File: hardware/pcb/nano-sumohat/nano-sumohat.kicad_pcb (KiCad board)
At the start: 2 copper layers, 59.7 x 30.5 mm, 14 parts, among them J1 Analog, J10 H-OUT, J2 Digital, J4 IR-B, J5 IR-F, J6 UltrSnd, J7 H, J8 IR-START, J9 BAT-IN, SW1 Power SW

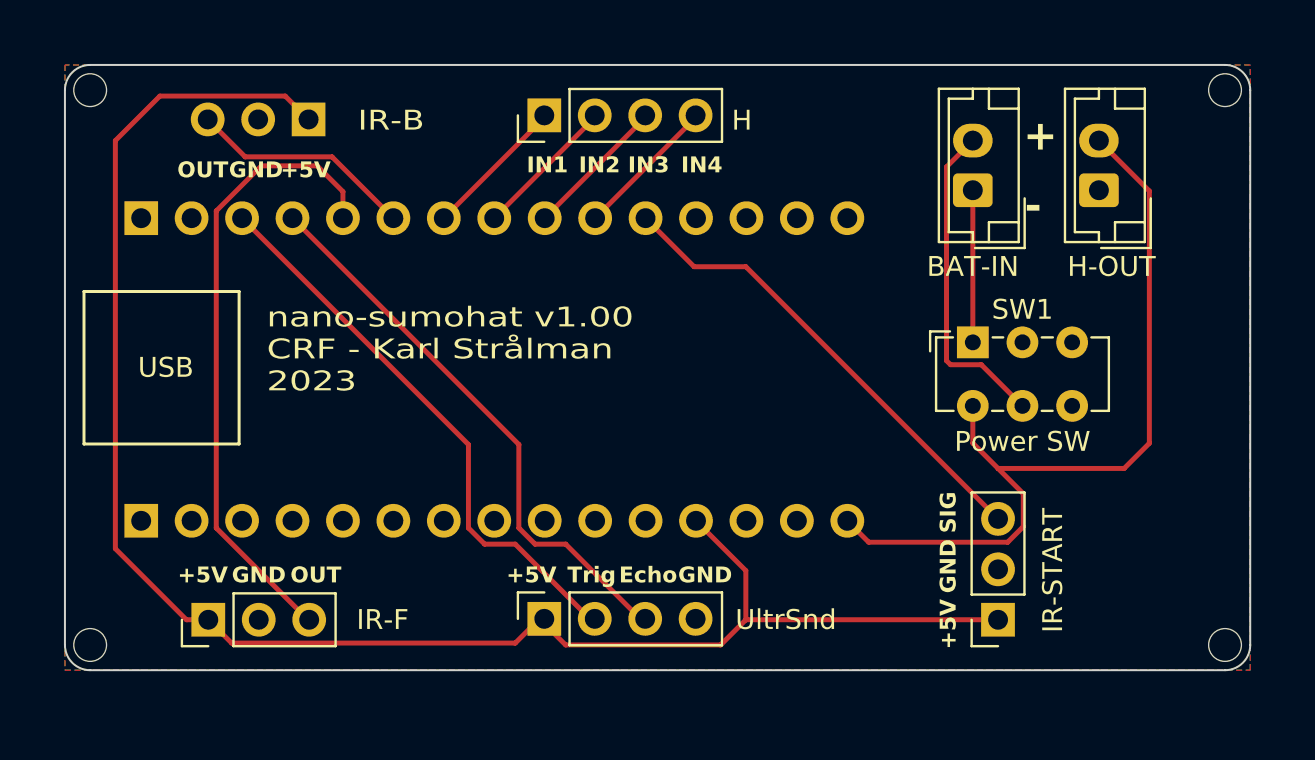
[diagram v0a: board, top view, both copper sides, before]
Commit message: Add v1.1 for nano sumohat
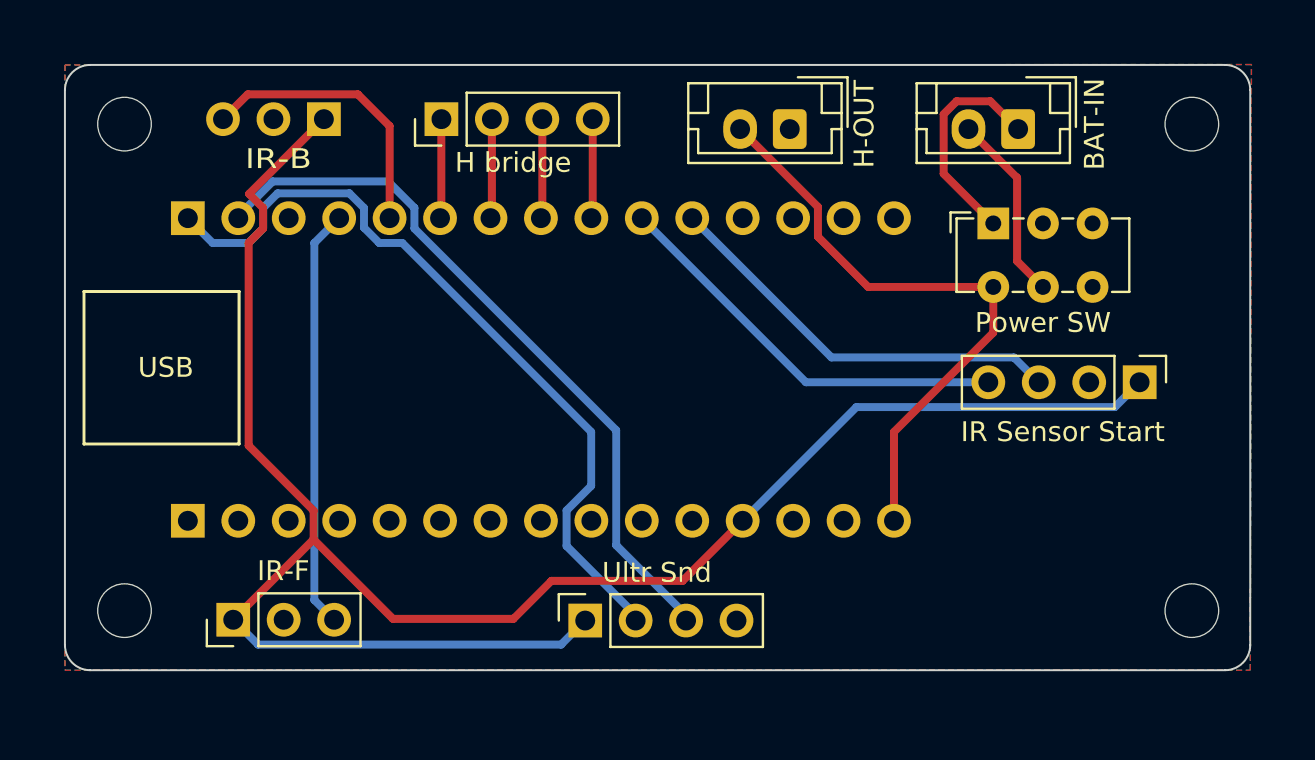
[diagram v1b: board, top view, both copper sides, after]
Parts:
- removed J8: IR-START, Connector_PinSocket_2.54mm:PinSocket_1x03_P2.54mm_Vertical
- removed MH1, MH2, MH3, MH4: MountingHole_65mil, Arduino_MountingHole:MountingHole_65mil
- added G***: LOGO, crf:crf_15x15, B.Cu at (116.8, 85.0)
- added J3: IR Sensor Start, Connector_PinHeader_2.54mm:PinHeader_1x04_P2.54mm_Vertical, F.Cu at (154.1, 85.5)
- added REF**: MountingHole_2.7mm_M2.5, MountingHole:MountingHole_2.7mm_M2.5, F.Cu at (156.8, 97.0)
- added REF**: MountingHole_2.7mm_M2.5, MountingHole:MountingHole_2.7mm_M2.5, F.Cu at (156.8, 72.5)
- added REF**: MountingHole_2.7mm_M2.5, MountingHole:MountingHole_2.7mm_M2.5, F.Cu at (103.0, 97.0)
- added REF**: MountingHole_2.7mm_M2.5, MountingHole:MountingHole_2.7mm_M2.5, F.Cu at (103.0, 72.5)
- J6: value UltrSnd -> Ultr Snd
- J7: value H -> H bridge
- moved J10 15.9 mm to (136.5, 72.8), turned to 180 degrees
- moved SW1 6.08 mm to (146.8, 77.5)
- moved J7 5.18 mm to (119.0, 72.2)
- moved J9 3.83 mm to (148.0, 72.8), turned to 180 degrees
- moved J1 2.35 mm to (106.2, 92.5)
- moved J2 2.35 mm to (106.2, 77.2)
- moved J6 2.06 mm to (126.2, 97.5)
- moved J5 1.25 mm to (108.5, 97.5)
- moved J4 0.77 mm to (113.0, 72.2)
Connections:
- J4 pad 3: /D7 -> /D8
- J5 pad 3: /D8 -> /*D9
- J6 pad 2: /*D10/SS -> /D12/MISO
- J6 pad 3: /*D9 -> /*D11/MOSI
- J7 pad 1: /*D6 -> /D7
- J7 pad 2: /*D5 -> /*D6
- J7 pad 3: /D4 -> /*D5
- J7 pad 4: /*D3 -> /D4
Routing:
- net /D12/MISO: track 0.00 -> 39.5 mm
- net /*D11/MOSI: track 0.00 -> 36.7 mm
- net /*D10/SS: track 28.3 -> 0.00 mm
- net /D8: track 31.8 -> 14.2 mm
- net /*D3: track 7.27 -> 20.9 mm
- net +5V: track 85.7 -> 97.3 mm
- net VCC: track 41.2 -> 30.8 mm
- net /*D9: track 28.3 -> 21.2 mm
- net /BAT_VCC: track 16.4 -> 9.50 mm
- net /D7: track 11.4 -> 5.02 mm
- net /BAT_GND: track 7.66 -> 11.1 mm
- net /D2: track 24.0 -> 20.9 mm
- net /*D6: track 7.27 -> 5.09 mm
- net /D4: track 7.27 -> 5.21 mm
- net /*D5: track 7.27 -> 5.28 mm
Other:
- board text added: "B_GND"
- board text added: "B_VCC"
- board text added: "Kill"
- board text added: "Start"
- board text added: "VCC"
- board text added: "nano-sumohat v1.1 Karl Strålman 2024-03"
- board text removed: "SIG"
- board text removed: "nano-sumohat v1.00 CRF - Karl Strålman 2023"

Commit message: Add v2-draft6 build guide
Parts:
- removed REF** (x4): MountingHole_2.7mm_M2.5, MountingHole:MountingHole_2.7mm_M2.5
- added G***: LOGO, crf:crf_15x15, F.Cu at (116.8, 85.0)
- added H1: MountingHole, MountingHole:MountingHole_2.7mm_M2.5_DIN965_Pad_TopBottom, F.Cu at (103.9, 87.5)
- added H2: MountingHole, MountingHole:MountingHole_2.7mm_M2.5_DIN965_Pad_TopBottom, F.Cu at (156.0, 73.1)
- added H3: MountingHole, MountingHole:MountingHole_2.7mm_M2.5_DIN965_Pad_TopBottom, F.Cu at (155.4, 87.5)
- added H4: MountingHole, MountingHole:MountingHole_2.7mm_M2.5_DIN965_Pad_TopBottom, F.Cu at (103.4, 72.9)
- added J8: Extension, Connector_PinHeader_2.54mm:PinHeader_2x05_P2.54mm_Vertical, F.Cu at (147.3, 97.5)
- added SW2: ~, Button_Switch_THT:SW_Slide-03_Wuerth-WS-SLTV_10x2.5x6.4_P2.54mm, F.Cu at (116.9, 97.5)
- J3: value IR Sensor Start -> IR_START
- J4: value IR-B -> IR_B
- J5: value IR-F -> IR_F
- J6: value Ultr Snd -> SND_Sensor
- J7: value H bridge -> Motor; footprint Connector_PinHeader_2.54mm:PinHeader_1x04_P2.54mm_Vertical -> Connector_PinHeader_2.54mm:PinHeader_1x06_P2.54mm_Vertical
- moved J4 21.1 mm to (134.1, 72.0)
- moved J7 6.26 mm to (112.7, 72.1)
- moved J5 5.50 mm to (103.0, 97.4)
- moved J10 5.36 mm to (141.8, 72.5)
- moved SW1 5.27 mm to (152.0, 77.0)
- moved J3 4.38 mm to (157.8, 83.0)
- moved J9 2.40 mm to (150.4, 72.5)
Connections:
- J3 pad 3: /D2 -> /START
- J7 pad 1: /D7 -> /A6
- J7 pad 2: /*D6 -> /D7
- J7 pad 3: /*D5 -> /*D6
- J7 pad 4: /D4 -> /*D5
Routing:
- net /D13/SCK: track 0.00 -> 67.6 mm, vias 0 -> 4
- net /*D10/SS: track 0.00 -> 66.8 mm, vias 0 -> 3
- net /START: track 0.00 -> 48.9 mm
- net /A2: track 0.00 -> 44.9 mm, vias 0 -> 2
- net /A0: track 0.00 -> 43.4 mm, vias 0 -> 2
- net /A3: track 0.00 -> 42.5 mm, vias 0 -> 3
- net /A1: track 0.00 -> 42.2 mm, vias 0 -> 5
- net /A5/SCL: track 0.00 -> 42.1 mm, vias 0 -> 5
- net /A4/SDA: track 0.00 -> 34.4 mm, vias 0 -> 1
- net /A6: track 0.00 -> 30.6 mm
- net +5V: track 97.3 -> 73.0 mm
- net /D0/RX: track 0.00 -> 24.0 mm, vias 0 -> 2
- net /A7: track 0.00 -> 23.0 mm
- net /D1/TX: track 0.00 -> 20.1 mm, vias 0 -> 2
- net /D8: track 14.2 -> 0.00 mm
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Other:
- board text added: "ENA"
- board text added: "ENB"
- board text added: "Start SEL"
- board text added: "nano-sumohat v1.2 Karl Strålman 2024-09"
- board text removed: "USB"
- board text removed: "nano-sumohat v1.1 Karl Strålman 2024-03"

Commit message: Update PCB v1.2
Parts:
- SW1: value Power SW -> ~; footprint Button_Switch_THT:SW_E-Switch_EG1271_SPDT -> Button_Switch_THT:SW_Slide-03_Wuerth-WS-SLTV_10x2.5x6.4_P2.54mm
- moved SW1 2.90 mm to (153.5, 79.5)
- moved H1 0.63 mm to (103.5, 88.0)
- moved H2 0.51 mm to (156.5, 73.0)
- moved H3 0.51 mm to (155.5, 88.0)
- moved H4 0.17 mm to (103.5, 73.0)
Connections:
- J9 pad 1: /BAT_GND -> GND
- SW1 pad 1: /BAT_GND -> /BAT_VCC
- SW1 pad 2: GND -> unconnected-(SW1-C-Pad2)
- SW1 pad 3: unconnected-(SW1-Pad3) -> VCC
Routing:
- net /D8: track 0.00 -> 17.2 mm, vias 0 -> 2
- net GND: track 0.00 -> 13.6 mm, vias 0 -> 163
- net +5V: track 73.0 -> 82.2 mm, vias 0 -> 2
- net /BAT_GND: track 5.12 -> 0.00 mm
- net VCC: track 33.2 -> 37.7 mm
- net /A5/SCL: track 42.1 -> 45.2 mm
- net /BAT_VCC: track 11.7 -> 9.26 mm
- net /START: track 48.9 -> 46.8 mm
- net /A6: track 30.6 -> 28.8 mm
- net /D13/SCK: track 67.6 -> 66.7 mm
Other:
- board text added: "A0"
- board text added: "A1"
- board text added: "A2"
- board text added: "A3"
- board text added: "A4"
- board text added: "A5"
- board text added: "BATTERY"
- board text added: "D0"
- board text added: "D1"
- board text added: "D10"
- board text added: "D13"
- board text added: "Ext."
- board text added: "IR_B"
- board text added: "IR_F"
- board text added: "JLCJLCJLCJLC"
- board text added: "Motor_Driver"
- board text added: "ON/OFF"
- board text added: "SEL"
- board text added: "START"
- board text added: "ULTR_SND"
- board text added: "VCC OUT"
- board text added: "x"
